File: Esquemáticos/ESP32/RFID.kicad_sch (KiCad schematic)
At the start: 1 part

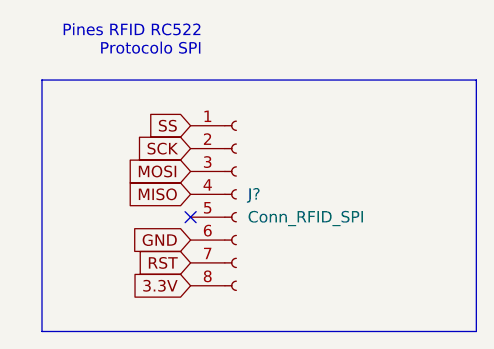
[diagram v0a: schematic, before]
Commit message: Añadido Modo Programación
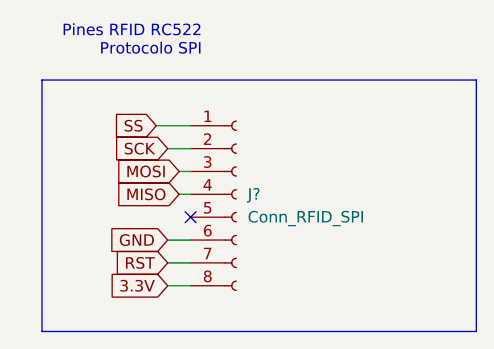
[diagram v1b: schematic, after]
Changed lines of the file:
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@@
   (paper "A4")
   (no_connect (at 97.79 58.42))
+  (wire (pts (xy 95.25 50.8) (xy 97.79 50.8))
+    (stroke (width 0) (type default) (color 0 0 0 0))
+  )
   (polyline (pts (xy 81.28 71.12) (xy 81.28 43.18))
+    (stroke (width 0) (type default) (color 0 0 0 0))
+  )
+  (wire (pts (xy 95.25 63.5) (xy 97.79 63.5))
     (stroke (width 0) (type default) (color 0 0 0 0))
   )
@@
     (stroke (width 0) (type default) (color 0 0 0 0))
   )
+  (wire (pts (xy 95.25 66.04) (xy 97.79 66.04))
+    (stroke (width 0) (type default) (color 0 0 0 0))
+  )
   (polyline (pts (xy 129.54 43.18) (xy 129.54 71.12))
+    (stroke (width 0) (type default) (color 0 0 0 0))
+  )
+  (wire (pts (xy 96.52 55.88) (xy 97.79 55.88))
     (stroke (width 0) (type default) (color 0 0 0 0))
   )
@@
     (stroke (width 0) (type default) (color 0 0 0 0))
   )
+  (wire (pts (xy 96.52 53.34) (xy 97.79 53.34))
+    (stroke (width 0) (type default) (color 0 0 0 0))
+  )
+  (wire (pts (xy 95.25 60.96) (xy 97.79 60.96))
+    (stroke (width 0) (type default) (color 0 0 0 0))
+  )
+  (wire (pts (xy 93.98 48.26) (xy 97.79 48.26))
+    (stroke (width 0) (type default) (color 0 0 0 0))
+  )
   (text "Pines RFID RC522\nProtocolo SPI" (at 99.06 40.64 180)
     (effects (font (size 1.27 1.27)) (justify right bottom))
   )
-  (global_label "MISO" (shape input) (at 97.79 55.88 180) (fields_autoplaced)
+  (global_label "MISO" (shape input) (at 96.52 55.88 180) (fields_autoplaced)
     (effects (font (size 1.27 1.27)) (justify right))
-    (property "Referencias entre hojas" "${INTERSHEET_REFS}" (id 0) (at 90.7807 55.8006 0)
+    (property "Referencias entre hojas" "${INTERSHEET_REFS}" (id 0) (at 89.5107 55.8006 0)
       (effects (font (size 1.27 1.27)) (justify right) hide)
     )
   )
-  (global_label "3.3V" (shape input) (at 97.79 66.04 180) (fields_autoplaced)
+  (global_label "3.3V" (shape input) (at 95.25 66.04 180) (fields_autoplaced)
     (effects (font (size 1.27 1.27)) (justify right))
-    (property "Referencias entre hojas" "${INTERSHEET_REFS}" (id 0) (at 91.2645 65.9606 0)
+    (property "Referencias entre hojas" "${INTERSHEET_REFS}" (id 0) (at 88.7245 65.9606 0)
       (effects (font (size 1.27 1.27)) (justify right) hide)
     )
   )
-  (global_label "SS" (shape input) (at 97.79 48.26 180) (fields_autoplaced)
+  (global_label "SS" (shape input) (at 93.98 48.26 180) (fields_autoplaced)
     (effects (font (size 1.27 1.27)) (justify right))
-    (property "Referencias entre hojas" "${INTERSHEET_REFS}" (id 0) (at 92.9579 48.1806 0)
+    (property "Referencias entre hojas" "${INTERSHEET_REFS}" (id 0) (at 89.1479 48.1806 0)
       (effects (font (size 1.27 1.27)) (justify right) hide)
     )
   )
-  (global_label "MOSI" (shape input) (at 97.79 53.34 180) (fields_autoplaced)
+  (global_label "MOSI" (shape input) (at 96.52 53.34 180) (fields_autoplaced)
     (effects (font (size 1.27 1.27)) (justify right))
-    (property "Referencias entre hojas" "${INTERSHEET_REFS}" (id 0) (at 90.7807 53.2606 0)
+    (property "Referencias entre hojas" "${INTERSHEET_REFS}" (id 0) (at 89.5107 53.2606 0)
       (effects (font (size 1.27 1.27)) (justify right) hide)
     )
   )
-  (global_label "RST" (shape input) (at 97.79 63.5 180) (fields_autoplaced)
+  (global_label "RST" (shape input) (at 95.25 63.5 180) (fields_autoplaced)
     (effects (font (size 1.27 1.27)) (justify right))
-    (property "Referencias entre hojas" "${INTERSHEET_REFS}" (id 0) (at 91.9298 63.4206 0)
+    (property "Referencias entre hojas" "${INTERSHEET_REFS}" (id 0) (at 89.3898 63.4206 0)
       (effects (font (size 1.27 1.27)) (justify right) hide)
     )
   )
-  (global_label "GND" (shape input) (at 97.79 60.96 180) (fields_autoplaced)
+  (global_label "GND" (shape input) (at 95.25 60.96 180) (fields_autoplaced)
     (effects (font (size 1.27 1.27)) (justify right))
-    (property "Referencias entre hojas" "${INTERSHEET_REFS}" (id 0) (at 91.5064 60.8806 0)
+    (property "Referencias entre hojas" "${INTERSHEET_REFS}" (id 0) (at 88.9664 60.8806 0)
       (effects (font (size 1.27 1.27)) (justify right) hide)
     )
   )
-  (global_label "SCK" (shape input) (at 97.79 50.8 180) (fields_autoplaced)
+  (global_label "SCK" (shape input) (at 95.25 50.8 180) (fields_autoplaced)
     (effects (font (size 1.27 1.27)) (justify right))
-    (property "Referencias entre hojas" "${INTERSHEET_REFS}" (id 0) (at 91.6274 50.7206 0)
+    (property "Referencias entre hojas" "${INTERSHEET_REFS}" (id 0) (at 89.0874 50.7206 0)
       (effects (font (size 1.27 1.27)) (justify right) hide)
     )

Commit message: Cambios hechos al esquemático, faltan detalles
Revisar el discord para dejar todo al día con el feedback de hoy
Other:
- note added: "Conexiones para el módulo RFID"
- moved on the sheet: J?
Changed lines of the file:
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@@
 (kicad_sch (version 20211123) (generator eeschema)
   (paper "A4")
-  (no_connect (at 97.79 58.42))
-  (wire (pts (xy 95.25 50.8) (xy 97.79 50.8))
+  (no_connect (at 142.24 104.14))
+  (wire (pts (xy 140.97 96.52) (xy 142.24 96.52))
     (stroke (width 0) (type default) (color 0 0 0 0))
   )
-  (polyline (pts (xy 81.28 71.12) (xy 81.28 43.18))
+  (polyline (pts (xy 125.73 116.84) (xy 125.73 88.9))
     (stroke (width 0) (type default) (color 0 0 0 0))
   )
-  (wire (pts (xy 95.25 63.5) (xy 97.79 63.5))
+  (wire (pts (xy 140.97 109.22) (xy 142.24 109.22))
     (stroke (width 0) (type default) (color 0 0 0 0))
   )
-  (polyline (pts (xy 129.54 71.12) (xy 81.28 71.12))
+  (polyline (pts (xy 173.99 116.84) (xy 125.73 116.84))
     (stroke (width 0) (type default) (color 0 0 0 0))
   )
-  (wire (pts (xy 95.25 66.04) (xy 97.79 66.04))
+  (wire (pts (xy 140.97 111.76) (xy 142.24 111.76))
     (stroke (width 0) (type default) (color 0 0 0 0))
   )
-  (polyline (pts (xy 129.54 43.18) (xy 129.54 71.12))
+  (polyline (pts (xy 173.99 88.9) (xy 173.99 116.84))
     (stroke (width 0) (type default) (color 0 0 0 0))
   )
-  (wire (pts (xy 96.52 55.88) (xy 97.79 55.88))
+  (wire (pts (xy 140.97 101.6) (xy 142.24 101.6))
     (stroke (width 0) (type default) (color 0 0 0 0))
   )
-  (polyline (pts (xy 81.28 43.18) (xy 129.54 43.18))
+  (polyline (pts (xy 125.73 88.9) (xy 173.99 88.9))
     (stroke (width 0) (type default) (color 0 0 0 0))
   )
-  (wire (pts (xy 96.52 53.34) (xy 97.79 53.34))
+  (wire (pts (xy 140.97 99.06) (xy 142.24 99.06))
     (stroke (width 0) (type default) (color 0 0 0 0))
   )
-  (wire (pts (xy 95.25 60.96) (xy 97.79 60.96))
+  (wire (pts (xy 140.97 93.98) (xy 142.24 93.98))
     (stroke (width 0) (type default) (color 0 0 0 0))
   )
-  (wire (pts (xy 93.98 48.26) (xy 97.79 48.26))
-    (stroke (width 0) (type default) (color 0 0 0 0))
+  (text "Conexiones para el módulo RFID" (at 186.69 190.5 0)
+    (effects (font (size 1.27 1.27)) (justify left bottom))
   )
-  (text "Pines RFID RC522\nProtocolo SPI" (at 99.06 40.64 180)
+  (text "Pines RFID RC522\nProtocolo SPI" (at 143.51 86.36 180)
     (effects (font (size 1.27 1.27)) (justify right bottom))
   )
-  (global_label "MISO" (shape input) (at 96.52 55.88 180) (fields_autoplaced)
+  (hierarchical_label "MOSI" (shape output) (at 140.97 99.06 180)
     (effects (font (size 1.27 1.27)) (justify right))
-    (property "Referencias entre hojas" "${INTERSHEET_REFS}" (id 0) (at 89.5107 55.8006 0)
-      (effects (font (size 1.27 1.27)) (justify right) hide)
-    )
   )
-  (global_label "3.3V" (shape input) (at 95.25 66.04 180) (fields_autoplaced)
+  (hierarchical_label "MISO" (shape output) (at 140.97 101.6 180)
     (effects (font (size 1.27 1.27)) (justify right))
-    (property "Referencias entre hojas" "${INTERSHEET_REFS}" (id 0) (at 88.7245 65.9606 0)
-      (effects (font (size 1.27 1.27)) (justify right) hide)
-    )
   )
-  (global_label "SS" (shape input) (at 93.98 48.26 180) (fields_autoplaced)
+  (hierarchical_label "SS" (shape input) (at 140.97 93.98 180)
     (effects (font (size 1.27 1.27)) (justify right))
-    (property "Referencias entre hojas" "${INTERSHEET_REFS}" (id 0) (at 89.1479 48.1806 0)
-      (effects (font (size 1.27 1.27)) (justify right) hide)
-    )
   )
-  (global_label "MOSI" (shape input) (at 96.52 53.34 180) (fields_autoplaced)
+  (hierarchical_label "SCK" (shape input) (at 140.97 96.52 180)
     (effects (font (size 1.27 1.27)) (justify right))
-    (property "Referencias entre hojas" "${INTERSHEET_REFS}" (id 0) (at 89.5107 53.2606 0)
-      (effects (font (size 1.27 1.27)) (justify right) hide)
-    )
   )
-  (global_label "RST" (shape input) (at 95.25 63.5 180) (fields_autoplaced)
+  (hierarchical_label "3.3V" (shape input) (at 140.97 111.76 180)
     (effects (font (size 1.27 1.27)) (justify right))
-    (property "Referencias entre hojas" "${INTERSHEET_REFS}" (id 0) (at 89.3898 63.4206 0)
-      (effects (font (size 1.27 1.27)) (justify right) hide)
-    )
   )
-  (global_label "GND" (shape input) (at 95.25 60.96 180) (fields_autoplaced)
+  (hierarchical_label "RST" (shape input) (at 140.97 109.22 180)
     (effects (font (size 1.27 1.27)) (justify right))
-    (property "Referencias entre hojas" "${INTERSHEET_REFS}" (id 0) (at 88.9664 60.8806 0)
-      (effects (font (size 1.27 1.27)) (justify right) hide)
-    )
   )
-  (global_label "SCK" (shape input) (at 95.25 50.8 180) (fields_autoplaced)
-    (effects (font (size 1.27 1.27)) (justify right))
-    (property "Referencias entre hojas" "${INTERSHEET_REFS}" (id 0) (at 89.0874 50.7206 0)
-      (effects (font (size 1.27 1.27)) (justify right) hide)
-    )
-  )
-  (symbol (lib_id "Connector:Conn_01x08_Female") (at 102.87 55.88 0) (unit 1)
+  (symbol (lib_id "Connector:Conn_01x08_Female") (at 147.32 101.6 0) (unit 1)
     (in_bom yes) (on_board yes) (fields_autoplaced)
-    (property "Reference" "J?" (id 0) (at 104.14 55.8799 0)
+    (property "Reference" "J?" (id 0) (at 148.59 101.5999 0)
       (effects (font (size 1.27 1.27)) (justify left))
     )
-    (property "Value" "Conn_RFID_SPI" (id 1) (at 104.14 58.4199 0)
+    (property "Value" "Conn_RFID_SPI" (id 1) (at 148.59 104.1399 0)
       (effects (font (size 1.27 1.27)) (justify left))
     )
-    (property "Footprint" "" (id 2) (at 102.87 55.88 0)
+    (property "Footprint" "" (id 2) (at 147.32 101.6 0)
       (effects (font (size 1.27 1.27)) hide)
     )
-    (property "Datasheet" "~" (id 3) (at 102.87 55.88 0)
+    (property "Datasheet" "~" (id 3) (at 147.32 101.6 0)
       (effects (font (size 1.27 1.27)) hide)
     )
@@
     (pin "8")
   )
+  (symbol (lib_id "power:GND") (at 142.24 106.68 270) (unit 1)
+    (in_bom yes) (on_board yes) (fields_autoplaced)
+    (property "Reference" "#PWR?" (id 0) (at 135.89 106.68 0)
+      (effects (font (size 1.27 1.27)) hide)
+    )
+    (property "Value" "GND" (id 1) (at 138.43 106.6799 90)
+      (effects (font (size 1.27 1.27)) (justify right))
+    )
+    (property "Footprint" "" (id 2) (at 142.24 106.68 0)
+      (effects (font (size 1.27 1.27)) hide)
+    )
+    (property "Datasheet" "" (id 3) (at 142.24 106.68 0)
+      (effects (font (size 1.27 1.27)) hide)
+    )
+    (pin "1")
+  )
 )

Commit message: actualización raul
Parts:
- removed J?: Conn_RFID_SPI, symbol Connector:Conn_01x08_Female
- added U1: RFID_RC522, symbol libreria_raul:RFID_RC522
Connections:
- net 3.3V: now also U1.8 (3.3V)
- net GND: now also U1.6 (GND)
- net MISO: now also U1.4 (MISO)
- net MOSI: now also U1.3 (MOSI)
- net RST: now also U1.7 (RST)
- net SCK: now also U1.2 (SCK)
- net SS: now also U1.1 (SS)
- no-connect marks 1 -> 0
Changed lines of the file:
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@@
 (kicad_sch (version 20211123) (generator eeschema)
   (paper "A4")
-  (no_connect (at 142.24 104.14))
-  (wire (pts (xy 140.97 96.52) (xy 142.24 96.52))
+  (wire (pts (xy 133.35 99.06) (xy 134.62 99.06))
     (stroke (width 0) (type default) (color 0 0 0 0))
   )
@@
     (stroke (width 0) (type default) (color 0 0 0 0))
   )
-  (wire (pts (xy 140.97 109.22) (xy 142.24 109.22))
+  (wire (pts (xy 134.62 105.41) (xy 135.89 105.41))
     (stroke (width 0) (type default) (color 0 0 0 0))
   )
@@
     (stroke (width 0) (type default) (color 0 0 0 0))
   )
-  (wire (pts (xy 140.97 111.76) (xy 142.24 111.76))
+  (wire (pts (xy 133.35 106.68) (xy 134.62 106.68))
     (stroke (width 0) (type default) (color 0 0 0 0))
   )
@@
     (stroke (width 0) (type default) (color 0 0 0 0))
   )
-  (wire (pts (xy 140.97 101.6) (xy 142.24 101.6))
+  (wire (pts (xy 133.35 101.6) (xy 134.62 101.6))
     (stroke (width 0) (type default) (color 0 0 0 0))
   )
@@
     (stroke (width 0) (type default) (color 0 0 0 0))
   )
-  (wire (pts (xy 140.97 99.06) (xy 142.24 99.06))
+  (wire (pts (xy 133.35 100.33) (xy 134.62 100.33))
     (stroke (width 0) (type default) (color 0 0 0 0))
   )
-  (wire (pts (xy 140.97 93.98) (xy 142.24 93.98))
+  (wire (pts (xy 133.35 97.79) (xy 134.62 97.79))
     (stroke (width 0) (type default) (color 0 0 0 0))
   )
@@
     (effects (font (size 1.27 1.27)) (justify right bottom))
   )
-  (hierarchical_label "MOSI" (shape output) (at 140.97 99.06 180)
+  (hierarchical_label "MOSI" (shape output) (at 133.35 100.33 180)
     (effects (font (size 1.27 1.27)) (justify right))
   )
-  (hierarchical_label "MISO" (shape output) (at 140.97 101.6 180)
+  (hierarchical_label "MISO" (shape output) (at 133.35 101.6 180)
     (effects (font (size 1.27 1.27)) (justify right))
   )
-  (hierarchical_label "SS" (shape input) (at 140.97 93.98 180)
+  (hierarchical_label "SS" (shape input) (at 133.35 97.79 180)
     (effects (font (size 1.27 1.27)) (justify right))
   )
-  (hierarchical_label "SCK" (shape input) (at 140.97 96.52 180)
+  (hierarchical_label "SCK" (shape input) (at 133.35 99.06 180)
     (effects (font (size 1.27 1.27)) (justify right))
   )
-  (hierarchical_label "3.3V" (shape input) (at 140.97 111.76 180)
+  (hierarchical_label "3.3V" (shape input) (at 133.35 106.68 180)
     (effects (font (size 1.27 1.27)) (justify right))
   )
-  (hierarchical_label "RST" (shape input) (at 140.97 109.22 180)
+  (hierarchical_label "RST" (shape input) (at 134.62 105.41 180)
     (effects (font (size 1.27 1.27)) (justify right))
   )
-  (symbol (lib_id "Connector:Conn_01x08_Female") (at 147.32 101.6 0) (unit 1)
+  (symbol (lib_id "libreria_raul:RFID_RC522") (at 146.05 93.98 0) (unit 1)
     (in_bom yes) (on_board yes) (fields_autoplaced)
-    (property "Reference" "J?" (id 0) (at 148.59 101.5999 0)
+    (property "Reference" "U1" (id 0) (at 160.02 101.5999 0)
       (effects (font (size 1.27 1.27)) (justify left))
     )
-    (property "Value" "Conn_RFID_SPI" (id 1) (at 148.59 104.1399 0)
+    (property "Value" "RFID_RC522" (id 1) (at 160.02 104.1399 0)
       (effects (font (size 1.27 1.27)) (justify left))
     )
-    (property "Footprint" "" (id 2) (at 147.32 101.6 0)
+    (property "Footprint" "" (id 2) (at 146.05 93.98 0)
       (effects (font (size 1.27 1.27)) hide)
     )
-    (property "Datasheet" "~" (id 3) (at 147.32 101.6 0)
+    (property "Datasheet" "" (id 3) (at 146.05 93.98 0)
       (effects (font (size 1.27 1.27)) hide)
     )
@@
     (pin "8")
   )
-  (symbol (lib_id "power:GND") (at 142.24 106.68 270) (unit 1)
+  (symbol (lib_id "power:GND") (at 134.62 104.14 270) (unit 1)
     (in_bom yes) (on_board yes) (fields_autoplaced)
-    (property "Reference" "#PWR?" (id 0) (at 135.89 106.68 0)
+    (property "Reference" "#PWR?" (id 0) (at 128.27 104.14 0)
       (effects (font (size 1.27 1.27)) hide)
     )
-    (property "Value" "GND" (id 1) (at 138.43 106.6799 90)
+    (property "Value" "GND" (id 1) (at 130.81 104.1399 90)
       (effects (font (size 1.27 1.27)) (justify right))
     )
-    (property "Footprint" "" (id 2) (at 142.24 106.68 0)
+    (property "Footprint" "" (id 2) (at 134.62 104.14 0)
       (effects (font (size 1.27 1.27)) hide)
     )
-    (property "Datasheet" "" (id 3) (at 142.24 106.68 0)
+    (property "Datasheet" "" (id 3) (at 134.62 104.14 0)
       (effects (font (size 1.27 1.27)) hide)
     )
